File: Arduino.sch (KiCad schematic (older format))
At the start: 16 parts

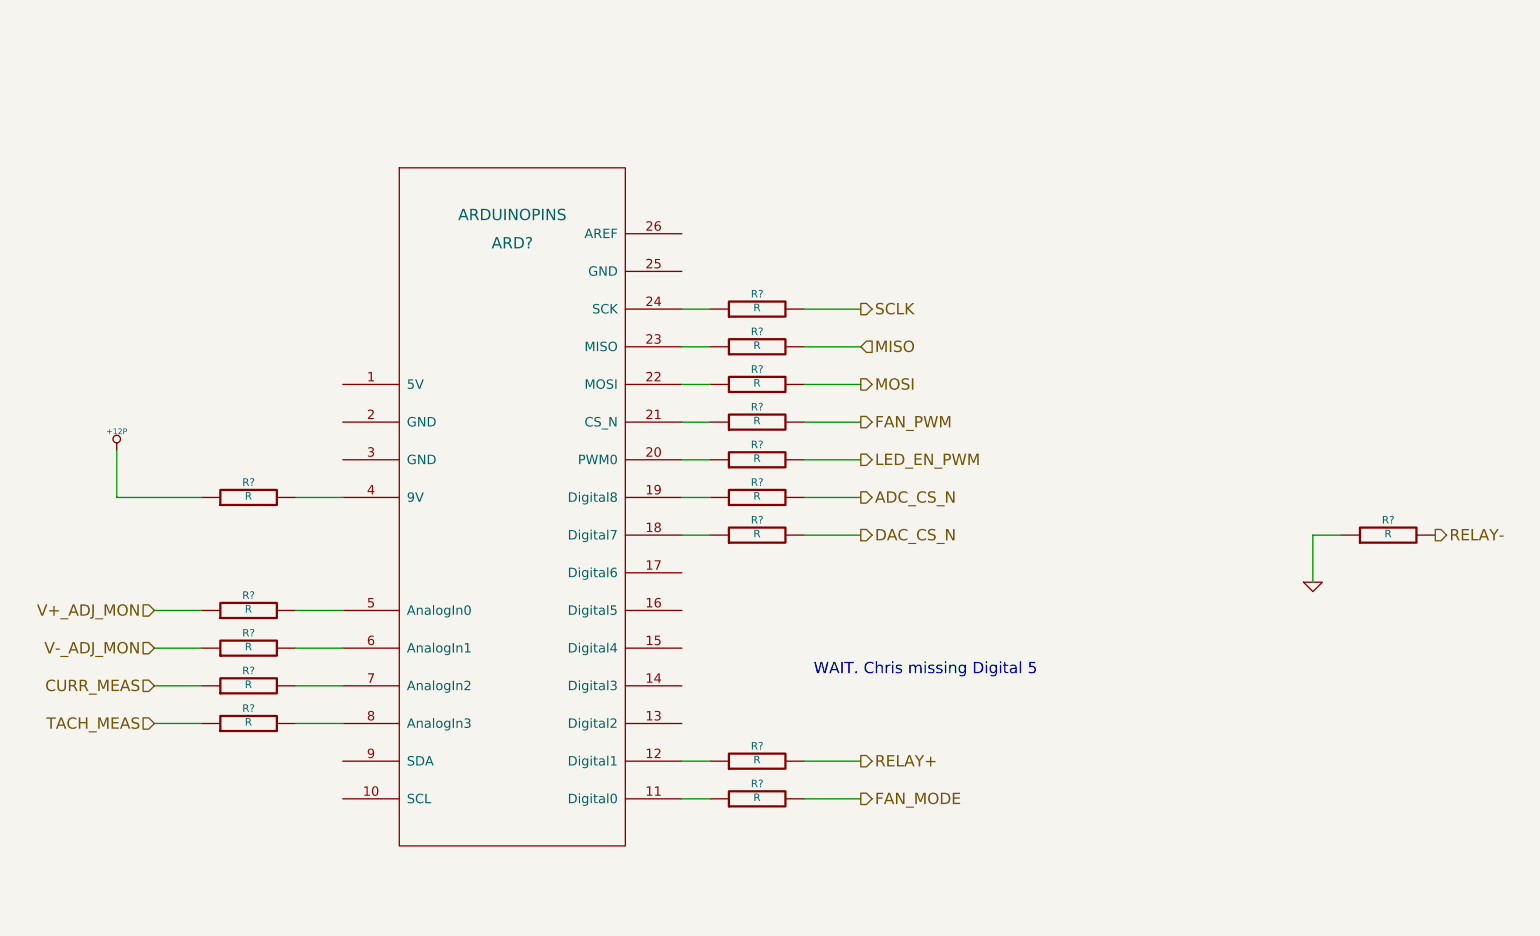
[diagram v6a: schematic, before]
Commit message: Initial Relay PCB Layout
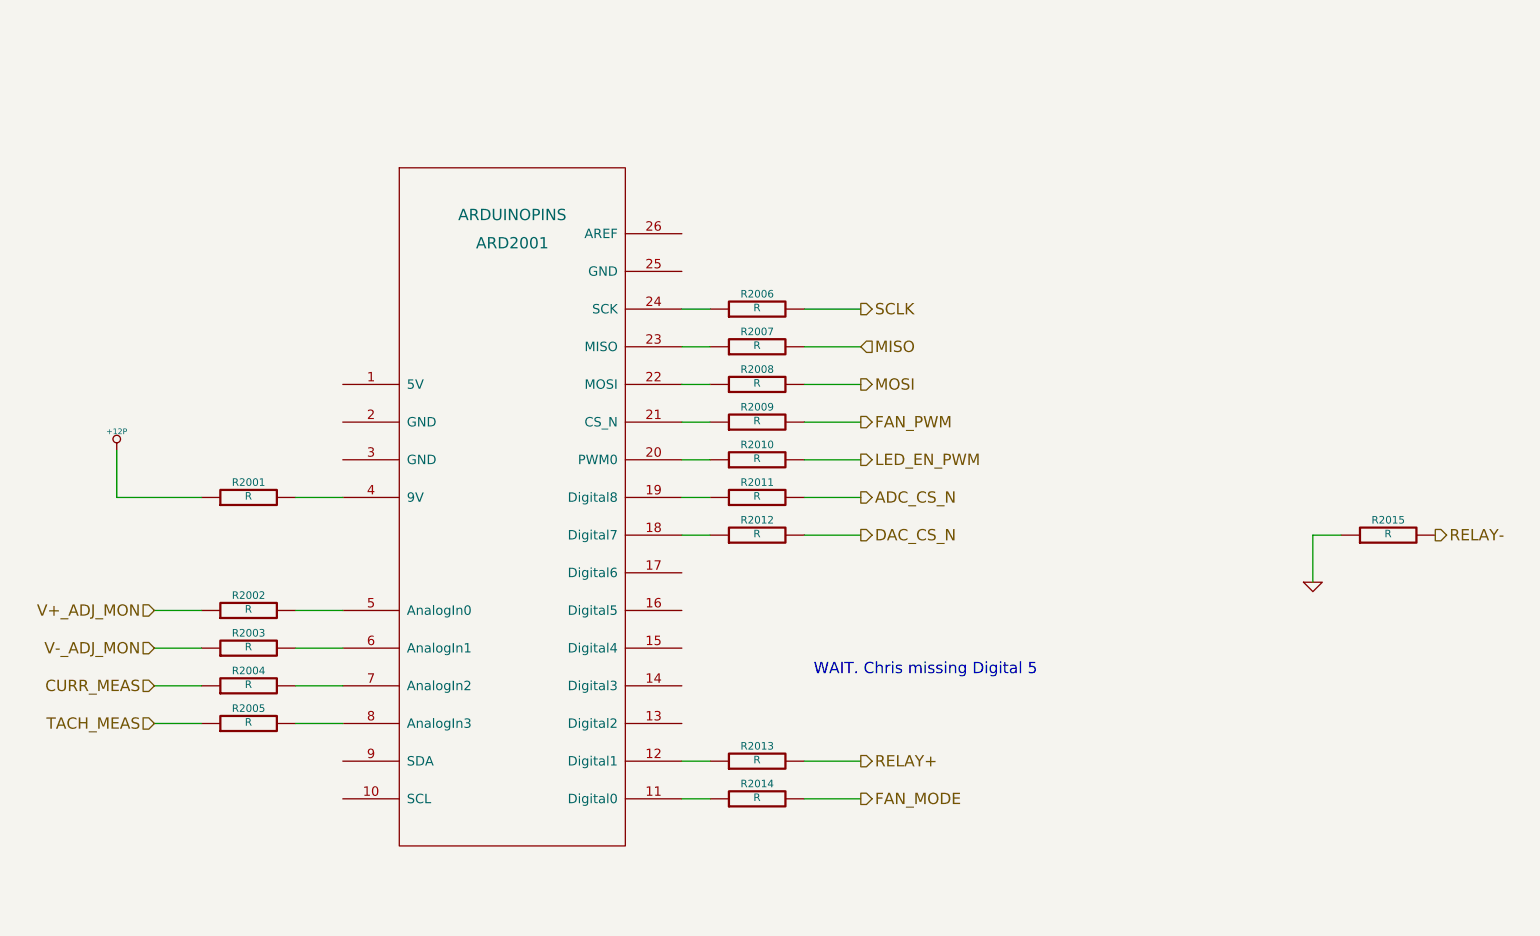
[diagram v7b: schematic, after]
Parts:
- gave numbers to parts that had none: 16
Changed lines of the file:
@@
 Sheet 2 9
 Title ""
-Date "9 feb 2014"
+Date "17 feb 2014"
 Rev ""
 Comp ""
@@
 CURR_MEAS
 $Comp
-L R R?
+L R R2009
 U 1 1 52F32414
 P 6450 3850
-F 0 "R?" V 6530 3850 40  0000 C CNN
+F 0 "R2009" V 6530 3850 40  0000 C CNN
 F 1 "R" V 6457 3851 40  0000 C CNN
 F 2 "~" V 6380 3850 30  0000 C CNN
@@
 $EndComp
 $Comp
-L R R?
+L R R2013
 U 1 1 52F3243B
 P 6450 5650
-F 0 "R?" V 6530 5650 40  0000 C CNN
+F 0 "R2013" V 6530 5650 40  0000 C CNN
 F 1 "R" V 6457 5651 40  0000 C CNN
 F 2 "~" V 6380 5650 30  0000 C CNN
@@
 $EndComp
 $Comp
-L GND #PWR?
+L GND #PWR2002
 U 1 1 52F33146
 P 9400 4700
-F 0 "#PWR?" H 9400 4700 30  0001 C CNN
+F 0 "#PWR2002" H 9400 4700 30  0001 C CNN
 F 1 "GND" H 9400 4630 30  0001 C CNN
 F 2 "" H 9400 4700 60  0000 C CNN
@@
 	6050 3850 6200 3850
 $Comp
-L R R?
+L R R2004
 U 1 1 52F3385F
 P 3750 5250
-F 0 "R?" V 3830 5250 40  0000 C CNN
+F 0 "R2004" V 3830 5250 40  0000 C CNN
 F 1 "R" V 3757 5251 40  0000 C CNN
 F 2 "~" V 3680 5250 30  0000 C CNN
@@
 $EndComp
 $Comp
-L R R?
+L R R2005
 U 1 1 52F33865
 P 3750 5450
-F 0 "R?" V 3830 5450 40  0000 C CNN
+F 0 "R2005" V 3830 5450 40  0000 C CNN
 F 1 "R" V 3757 5451 40  0000 C CNN
 F 2 "~" V 3680 5450 30  0000 C CNN
@@
 V-_ADJ_MON
 $Comp
-L R R?
+L R R2003
 U 1 1 52F349C2
 P 3750 5050
-F 0 "R?" V 3830 5050 40  0000 C CNN
+F 0 "R2003" V 3830 5050 40  0000 C CNN
 F 1 "R" V 3757 5051 40  0000 C CNN
 F 2 "~" V 3680 5050 30  0000 C CNN
@@
 $EndComp
 $Comp
-L R R?
+L R R2002
 U 1 1 52F349C8
 P 3750 4850
-F 0 "R?" V 3830 4850 40  0000 C CNN
+F 0 "R2002" V 3830 4850 40  0000 C CNN
 F 1 "R" V 3757 4851 40  0000 C CNN
 F 2 "~" V 3680 4850 30  0000 C CNN
@@
 	4250 4850 4000 4850
 $Comp
-L R R?
+L R R2012
 U 1 1 52F34A10
 P 6450 4450
-F 0 "R?" V 6530 4450 40  0000 C CNN
+F 0 "R2012" V 6530 4450 40  0000 C CNN
 F 1 "R" V 6457 4451 40  0000 C CNN
 F 2 "~" V 6380 4450 30  0000 C CNN
@@
 $EndComp
 $Comp
-L R R?
+L R R2008
 U 1 1 52F34A16
 P 6450 3650
-F 0 "R?" V 6530 3650 40  0000 C CNN
+F 0 "R2008" V 6530 3650 40  0000 C CNN
 F 1 "R" V 6457 3651 40  0000 C CNN
 F 2 "~" V 6380 3650 30  0000 C CNN
@@
 $EndComp
 $Comp
-L R R?
+L R R2007
 U 1 1 52F34A1C
 P 6450 3450
-F 0 "R?" V 6530 3450 40  0000 C CNN
+F 0 "R2007" V 6530 3450 40  0000 C CNN
 F 1 "R" V 6457 3451 40  0000 C CNN
 F 2 "~" V 6380 3450 30  0000 C CNN
@@
 $EndComp
 $Comp
-L R R?
+L R R2006
 U 1 1 52F34A22
 P 6450 3250
-F 0 "R?" V 6530 3250 40  0000 C CNN
+F 0 "R2006" V 6530 3250 40  0000 C CNN
 F 1 "R" V 6457 3251 40  0000 C CNN
 F 2 "~" V 6380 3250 30  0000 C CNN
@@
 	6050 4450 6200 4450
 $Comp
-L R R?
+L R R2015
 U 1 1 52F34ADA
 P 9800 4450
-F 0 "R?" V 9880 4450 40  0000 C CNN
+F 0 "R2015" V 9880 4450 40  0000 C CNN
 F 1 "R" V 9807 4451 40  0000 C CNN
 F 2 "~" V 9730 4450 30  0000 C CNN
@@
 $EndComp
 $Comp
-L R R?
+L R R2010
 U 1 1 52F34AE7
 P 6450 4050
-F 0 "R?" V 6530 4050 40  0000 C CNN
+F 0 "R2010" V 6530 4050 40  0000 C CNN
 F 1 "R" V 6457 4051 40  0000 C CNN
 F 2 "~" V 6380 4050 30  0000 C CNN
@@
 ADC_CS_N
 $Comp
-L R R?
+L R R2011
 U 1 1 52F37027
 P 6450 4250
-F 0 "R?" V 6530 4250 40  0000 C CNN
+F 0 "R2011" V 6530 4250 40  0000 C CNN
 F 1 "R" V 6457 4251 40  0000 C CNN
 F 2 "~" V 6380 4250 30  0000 C CNN
@@
 	6700 5850 7000 5850
 $Comp
-L R R?
+L R R2014
 U 1 1 52F7B7CD
 P 6450 5850
-F 0 "R?" V 6530 5850 40  0000 C CNN
+F 0 "R2014" V 6530 5850 40  0000 C CNN
 F 1 "R" V 6457 5851 40  0000 C CNN
 F 2 "~" V 6380 5850 30  0000 C CNN
@@
 WAIT. Chris missing Digital 5
 $Comp
-L R R?
+L R R2001
 U 1 1 52F7B7D5
 P 3750 4250
-F 0 "R?" V 3830 4250 40  0000 C CNN
+F 0 "R2001" V 3830 4250 40  0000 C CNN
 F 1 "R" V 3757 4251 40  0000 C CNN
 F 2 "~" V 3680 4250 30  0000 C CNN
@@
 	4250 4250 4000 4250
 $Comp
-L +12P #PWR?
+L +12P #PWR2001
 U 1 1 52F7B7FA
 P 3050 4000
-F 0 "#PWR?" H 3050 3970 30  0001 C CNN
+F 0 "#PWR2001" H 3050 3970 30  0001 C CNN
 F 1 "+12P" H 3050 4100 30  0000 C CNN
 F 2 "" H 3050 4000 60  0000 C CNN
@@
 	3050 4250 3500 4250
 $Comp
-L ARDUINOPINS ARD?
+L ARDUINOPINS ARD2001
 U 1 1 52F7C9A3
 P 5200 4200
-F 0 "ARD?" H 5150 5500 60  0000 C CNN
+F 0 "ARD2001" H 5150 5500 60  0000 C CNN
 F 1 "ARDUINOPINS" H 5150 5650 60  0000 C CNN
 F 2 "~" H 4900 4450 60  0000 C CNN

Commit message: Added Arduino Connect Pin Layout
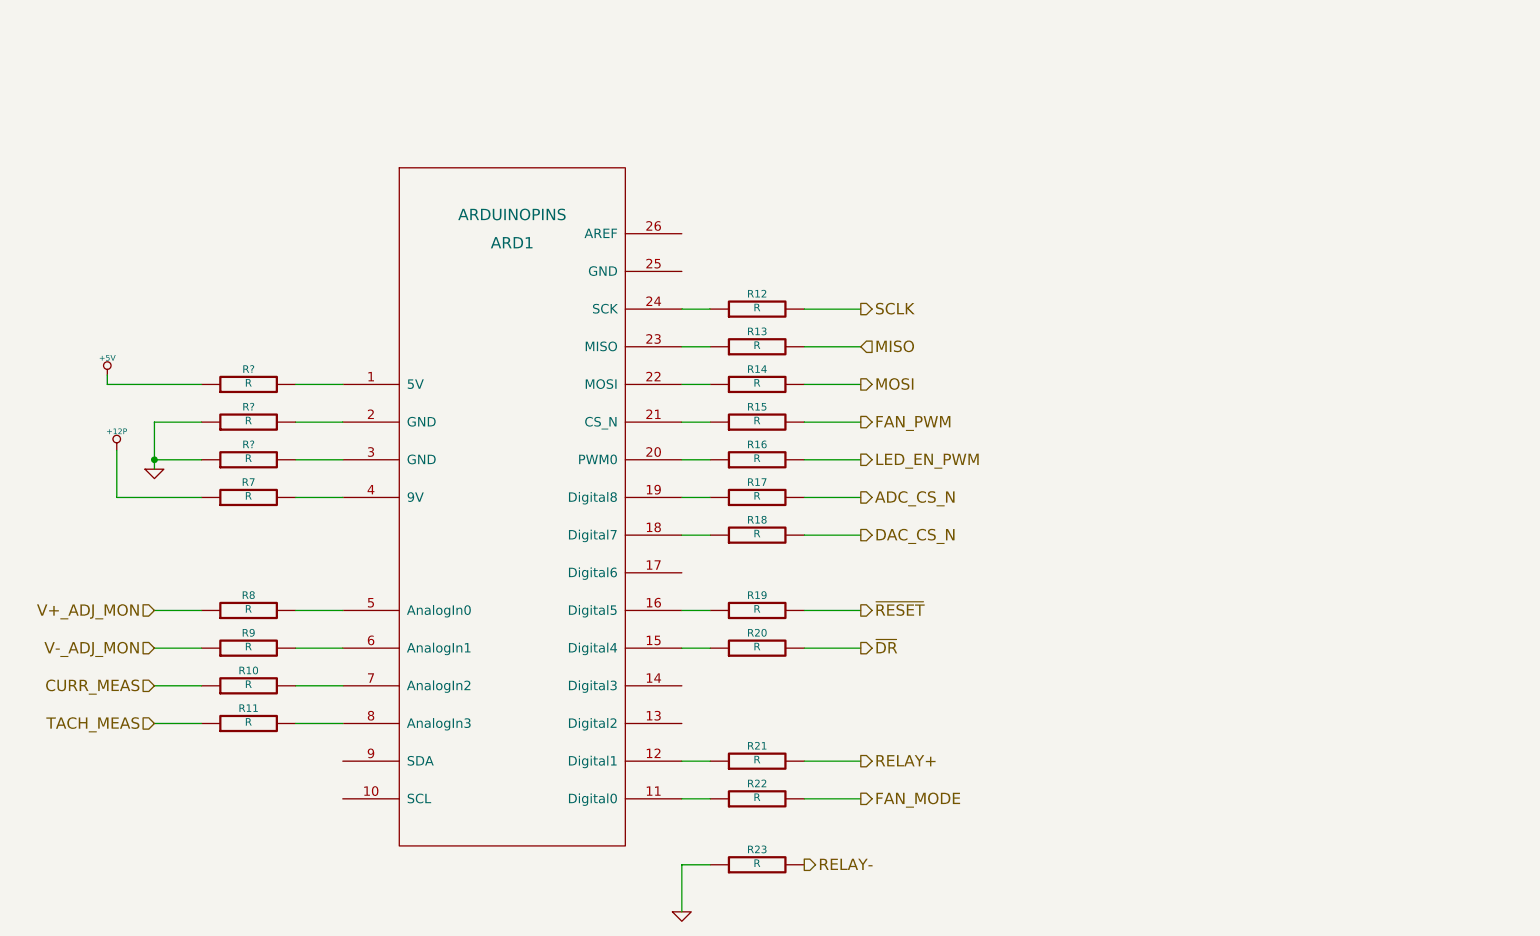
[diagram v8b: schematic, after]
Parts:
- added R19, R20, R? (x3): R, ~, symbol R
- renumbered ARD2001 to ARD1, R2004 to R10, R2005 to R11, R2006 to R12, R2007 to R13, R2008 to R14, R2009 to R15, R2010 to R16, R2011 to R17, R2012 to R18, R2013 to R21, R2014 to R22, R2015 to R23, R2001 to R7, R2002 to R8, R2003 to R9
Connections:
- net GND: now also R?.1, R?.1
- net at ARD1.1 (5V): now also R?.2
- net at ARD1.15 (Digital4): now also R20.1
- net at ARD1.16 (Digital5): now also R19.1
- net at ARD1.2 (GND): now also R?.2
- net at ARD1.3 (GND): now also R?.2
- new net +5V: R?.1
- new net ~DR: R20.2
- new net ~RESET: R19.2
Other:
- note removed: "WAIT. Chris missing Digital 5"
- moved on the sheet: R23
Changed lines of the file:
@@
 Sheet 2 9
 Title ""
-Date "17 feb 2014"
+Date "20 feb 2014"
 Rev ""
 Comp ""
@@
 Text HLabel 7000 5650 2    60   Output ~ 0
 RELAY+
-Text HLabel 10050 4450 2    60   Output ~ 0
+Text HLabel 6700 6200 2    60   Output ~ 0
 RELAY-
 Text HLabel 7000 3650 2    60   Output ~ 0
@@
 CURR_MEAS
 $Comp
-L R R2009
+L R R15
 U 1 1 52F32414
 P 6450 3850
-F 0 "R2009" V 6530 3850 40  0000 C CNN
+F 0 "R15" V 6530 3850 40  0000 C CNN
 F 1 "R" V 6457 3851 40  0000 C CNN
 F 2 "~" V 6380 3850 30  0000 C CNN
@@
 $EndComp
 $Comp
-L R R2013
+L R R21
 U 1 1 52F3243B
 P 6450 5650
-F 0 "R2013" V 6530 5650 40  0000 C CNN
+F 0 "R21" V 6530 5650 40  0000 C CNN
 F 1 "R" V 6457 5651 40  0000 C CNN
 F 2 "~" V 6380 5650 30  0000 C CNN
@@
 $EndComp
 $Comp
-L GND #PWR2002
+L GND #PWR2
 U 1 1 52F33146
-P 9400 4700
-F 0 "#PWR2002" H 9400 4700 30  0001 C CNN
-F 1 "GND" H 9400 4630 30  0001 C CNN
-F 2 "" H 9400 4700 60  0000 C CNN
-F 3 "" H 9400 4700 60  0000 C CNN
-	1    9400 4700
+P 6050 6450
+F 0 "#PWR2" H 6050 6450 30  0001 C CNN
+F 1 "GND" H 6050 6380 30  0001 C CNN
+F 2 "" H 6050 6450 60  0000 C CNN
+F 3 "" H 6050 6450 60  0000 C CNN
+	1    6050 6450
 	1    0    0    -1
 $EndComp
 Wire Wire Line
-	9550 4450 9400 4450
-Wire Wire Line
-	9400 4450 9400 4700
+	6200 6200 6050 6200
+Wire Wire Line
+	6050 6200 6050 6450
 Wire Wire Line
 	6700 3250 7000 3250
@@
 	6050 3850 6200 3850
 $Comp
-L R R2004
+L R R10
 U 1 1 52F3385F
 P 3750 5250
-F 0 "R2004" V 3830 5250 40  0000 C CNN
+F 0 "R10" V 3830 5250 40  0000 C CNN
 F 1 "R" V 3757 5251 40  0000 C CNN
 F 2 "~" V 3680 5250 30  0000 C CNN
@@
 $EndComp
 $Comp
-L R R2005
+L R R11
 U 1 1 52F33865
 P 3750 5450
-F 0 "R2005" V 3830 5450 40  0000 C CNN
+F 0 "R11" V 3830 5450 40  0000 C CNN
 F 1 "R" V 3757 5451 40  0000 C CNN
 F 2 "~" V 3680 5450 30  0000 C CNN
@@
 V-_ADJ_MON
 $Comp
-L R R2003
+L R R9
 U 1 1 52F349C2
 P 3750 5050
-F 0 "R2003" V 3830 5050 40  0000 C CNN
+F 0 "R9" V 3830 5050 40  0000 C CNN
 F 1 "R" V 3757 5051 40  0000 C CNN
 F 2 "~" V 3680 5050 30  0000 C CNN
@@
 $EndComp
 $Comp
-L R R2002
+L R R8
 U 1 1 52F349C8
 P 3750 4850
-F 0 "R2002" V 3830 4850 40  0000 C CNN
+F 0 "R8" V 3830 4850 40  0000 C CNN
 F 1 "R" V 3757 4851 40  0000 C CNN
 F 2 "~" V 3680 4850 30  0000 C CNN
@@
 	4250 4850 4000 4850
 $Comp
-L R R2012
+L R R18
 U 1 1 52F34A10
 P 6450 4450
-F 0 "R2012" V 6530 4450 40  0000 C CNN
+F 0 "R18" V 6530 4450 40  0000 C CNN
 F 1 "R" V 6457 4451 40  0000 C CNN
 F 2 "~" V 6380 4450 30  0000 C CNN
@@
 $EndComp
 $Comp
-L R R2008
+L R R14
 U 1 1 52F34A16
 P 6450 3650
-F 0 "R2008" V 6530 3650 40  0000 C CNN
+F 0 "R14" V 6530 3650 40  0000 C CNN
 F 1 "R" V 6457 3651 40  0000 C CNN
 F 2 "~" V 6380 3650 30  0000 C CNN
@@
 $EndComp
 $Comp
-L R R2007
+L R R13
 U 1 1 52F34A1C
 P 6450 3450
-F 0 "R2007" V 6530 3450 40  0000 C CNN
+F 0 "R13" V 6530 3450 40  0000 C CNN
 F 1 "R" V 6457 3451 40  0000 C CNN
 F 2 "~" V 6380 3450 30  0000 C CNN
@@
 $EndComp
 $Comp
-L R R2006
+L R R12
 U 1 1 52F34A22
 P 6450 3250
-F 0 "R2006" V 6530 3250 40  0000 C CNN
+F 0 "R12" V 6530 3250 40  0000 C CNN
 F 1 "R" V 6457 3251 40  0000 C CNN
 F 2 "~" V 6380 3250 30  0000 C CNN
@@
 	6050 4450 6200 4450
 $Comp
-L R R2015
+L R R23
 U 1 1 52F34ADA
-P 9800 4450
-F 0 "R2015" V 9880 4450 40  0000 C CNN
-F 1 "R" V 9807 4451 40  0000 C CNN
-F 2 "~" V 9730 4450 30  0000 C CNN
-F 3 "~" H 9800 4450 30  0000 C CNN
-	1    9800 4450
-	0    -1   -1   0
-$EndComp
-$Comp
-L R R2010
+P 6450 6200
+F 0 "R23" V 6530 6200 40  0000 C CNN
+F 1 "R" V 6457 6201 40  0000 C CNN
+F 2 "~" V 6380 6200 30  0000 C CNN
+F 3 "~" H 6450 6200 30  0000 C CNN
+	1    6450 6200
+	0    -1   -1   0
+$EndComp
+$Comp
+L R R16
 U 1 1 52F34AE7
 P 6450 4050
-F 0 "R2010" V 6530 4050 40  0000 C CNN
+F 0 "R16" V 6530 4050 40  0000 C CNN
 F 1 "R" V 6457 4051 40  0000 C CNN
 F 2 "~" V 6380 4050 30  0000 C CNN
@@
 ADC_CS_N
 $Comp
-L R R2011
+L R R17
 U 1 1 52F37027
 P 6450 4250
-F 0 "R2011" V 6530 4250 40  0000 C CNN
+F 0 "R17" V 6530 4250 40  0000 C CNN
 F 1 "R" V 6457 4251 40  0000 C CNN
 F 2 "~" V 6380 4250 30  0000 C CNN
@@
 	6700 5850 7000 5850
 $Comp
-L R R2014
+L R R22
 U 1 1 52F7B7CD
 P 6450 5850
-F 0 "R2014" V 6530 5850 40  0000 C CNN
+F 0 "R22" V 6530 5850 40  0000 C CNN
 F 1 "R" V 6457 5851 40  0000 C CNN
 F 2 "~" V 6380 5850 30  0000 C CNN
@@
 Wire Wire Line
 	6050 5850 6200 5850
-Text Notes 6750 5200 0    60   ~ 0
-WAIT. Chris missing Digital 5
-$Comp
-L R R2001
+$Comp
+L R R7
 U 1 1 52F7B7D5
 P 3750 4250
-F 0 "R2001" V 3830 4250 40  0000 C CNN
+F 0 "R7" V 3830 4250 40  0000 C CNN
 F 1 "R" V 3757 4251 40  0000 C CNN
 F 2 "~" V 3680 4250 30  0000 C CNN
@@
 	4250 4250 4000 4250
 $Comp
-L +12P #PWR2001
+L +12P #PWR1
 U 1 1 52F7B7FA
 P 3050 4000
-F 0 "#PWR2001" H 3050 3970 30  0001 C CNN
+F 0 "#PWR1" H 3050 3970 30  0001 C CNN
 F 1 "+12P" H 3050 4100 30  0000 C CNN
 F 2 "" H 3050 4000 60  0000 C CNN
@@
 	3050 4250 3500 4250
 $Comp
-L ARDUINOPINS ARD2001
+L ARDUINOPINS ARD1
 U 1 1 52F7C9A3
 P 5200 4200
-F 0 "ARD2001" H 5150 5500 60  0000 C CNN
+F 0 "ARD1" H 5150 5500 60  0000 C CNN
 F 1 "ARDUINOPINS" H 5150 5650 60  0000 C CNN
 F 2 "~" H 4900 4450 60  0000 C CNN
@@
 	1    0    0    -1
 $EndComp
+Text HLabel 7000 4850 2    60   Output ~ 0
+~RESET
+Text HLabel 7000 5050 2    60   Output ~ 0
+~DR
+$Comp
+L R R19
+U 1 1 53028F88
+P 6450 4850
+F 0 "R19" V 6530 4850 40  0000 C CNN
+F 1 "R" V 6457 4851 40  0000 C CNN
+F 2 "~" V 6380 4850 30  0000 C CNN
+F 3 "~" H 6450 4850 30  0000 C CNN
+	1    6450 4850
+	0    -1   -1   0
+$EndComp
+$Comp
+L R R20
+U 1 1 53028F8E
+P 6450 5050
+F 0 "R20" V 6530 5050 40  0000 C CNN
+F 1 "R" V 6457 5051 40  0000 C CNN
+F 2 "~" V 6380 5050 30  0000 C CNN
+F 3 "~" H 6450 5050 30  0000 C CNN
+	1    6450 5050
+	0    -1   -1   0
+$EndComp
+Wire Wire Line
+	6050 4850 6200 4850
+Wire Wire Line
+	6700 4850 7000 4850
+Wire Wire Line
+	7000 5050 6700 5050
+Wire Wire Line
+	6200 5050 6050 5050
+$Comp
+L R R?
+U 1 1 530561E5
+P 3750 4050
+F 0 "R?" V 3830 4050 40  0000 C CNN
+F 1 "R" V 3757 4051 40  0000 C CNN
+F 2 "~" V 3680 4050 30  0000 C CNN
+F 3 "~" H 3750 4050 30  0000 C CNN
+	1    3750 4050
+	0    -1   -1   0
+$EndComp
+$Comp
+L R R?
+U 1 1 530561EB
+P 3750 3850
+F 0 "R?" V 3830 3850 40  0000 C CNN
+F 1 "R" V 3757 3851 40  0000 C CNN
+F 2 "~" V 3680 3850 30  0000 C CNN
+F 3 "~" H 3750 3850 30  0000 C CNN
+	1    3750 3850
+	0    -1   -1   0
+$EndComp
+$Comp
+L R R?
+U 1 1 530561F1
+P 3750 3650
+F 0 "R?" V 3830 3650 40  0000 C CNN
+F 1 "R" V 3757 3651 40  0000 C CNN
+F 2 "~" V 3680 3650 30  0000 C CNN
+F 3 "~" H 3750 3650 30  0000 C CNN
+	1    3750 3650
+	0    -1   -1   0
+$EndComp
+$Comp
+L GND #PWR?
+U 1 1 53056214
+P 3250 4100
+F 0 "#PWR?" H 3250 4100 30  0001 C CNN
+F 1 "GND" H 3250 4030 30  0001 C CNN
+F 2 "" H 3250 4100 60  0000 C CNN
+F 3 "" H 3250 4100 60  0000 C CNN
+	1    3250 4100
+	1    0    0    -1
+$EndComp
+Wire Wire Line
+	3500 3850 3250 3850
+Wire Wire Line
+	3250 3850 3250 4100
+Wire Wire Line
+	3500 4050 3250 4050
+Connection ~ 3250 4050
+Wire Wire Line
+	4000 3850 4250 3850
+Wire Wire Line
+	4250 4050 4000 4050
+Wire Wire Line
+	4250 3650 4000 3650
+$Comp
+L +5V #PWR?
+U 1 1 5305636F
+P 3000 3600
+F 0 "#PWR?" H 3000 3690 20  0001 C CNN
+F 1 "+5V" H 3000 3690 30  0000 C CNN
+F 2 "" H 3000 3600 60  0000 C CNN
+F 3 "" H 3000 3600 60  0000 C CNN
+	1    3000 3600
+	1    0    0    -1
+$EndComp
+Wire Wire Line
+	3500 3650 3000 3650
+Wire Wire Line
+	3000 3650 3000 3600
 $EndSCHEMATC
